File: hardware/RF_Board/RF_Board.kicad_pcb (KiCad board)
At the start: 4 copper layers, 90 x 90 mm, 130 parts, among them J1 Conn_Coaxial, J2 Conn_01x04_Male, J3 Conn_Coaxial, J4 Conn_01x04_Male, J5 Conn_01x06_Female, J6 Conn_01x06_Female, J7 Conn_01x06_Female, J8 L77TSAH15SOL2RM8, Q1 2N7002, Q2 2N7002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

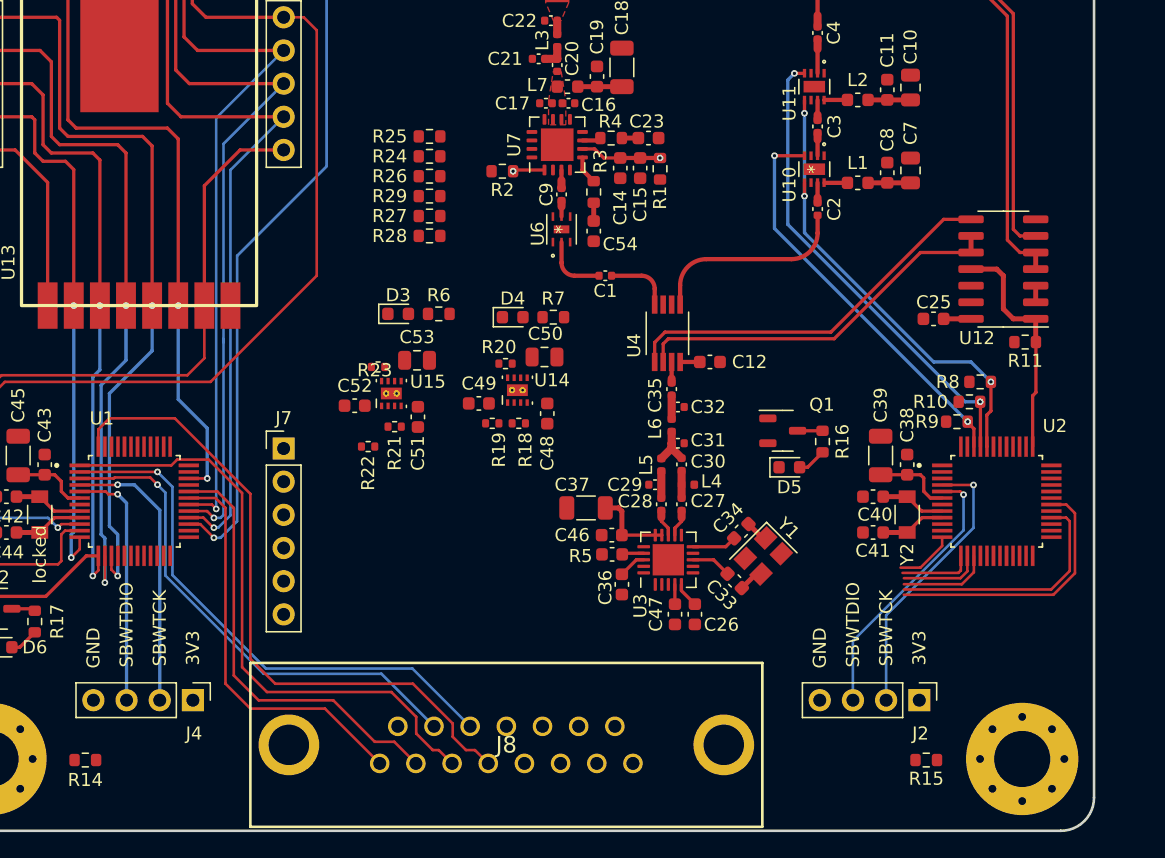
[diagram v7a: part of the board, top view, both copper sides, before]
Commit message: more RF board digital layout
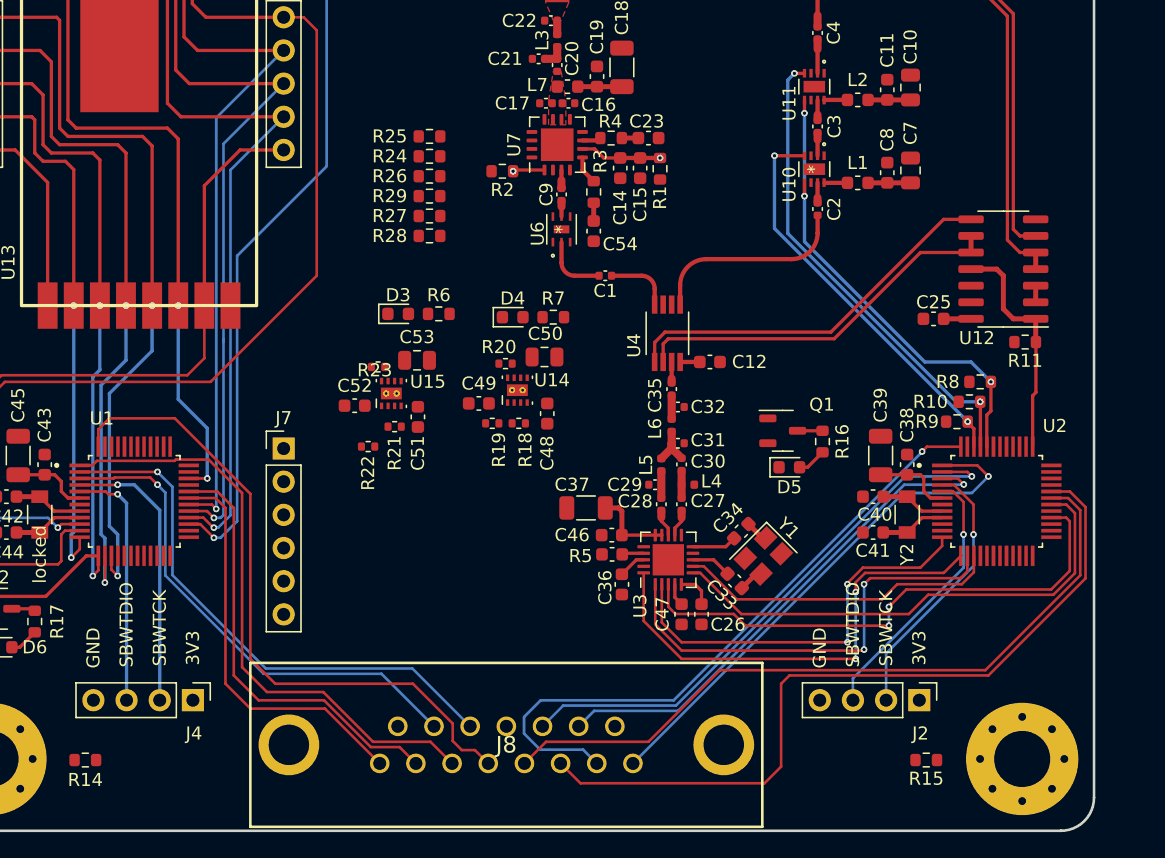
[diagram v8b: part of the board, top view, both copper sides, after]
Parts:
- moved C26 0.51 mm to (59.9, 73.4)
- moved C47 0.51 mm to (58.4, 73.4)
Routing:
- net /CC2500_UART_RX: track 0.00 -> 59.6 mm
- net /CC2500_UART_TX: track 0.00 -> 56.1 mm
- net /CC2500_TX_EMPTY: track 0.00 -> 49.8 mm, vias 0 -> 1
- net /CC2500_TX_OVERFLOW: track 0.00 -> 43.2 mm, vias 0 -> 1
- net /CC2500_RX_EMPTY: track 0.00 -> 40.2 mm, vias 0 -> 1
- net /CC2500_RX_OVERFLOW: track 0.00 -> 39.0 mm, vias 0 -> 1
- net /CC2500_MOSI: track 5.75 -> 36.0 mm, vias 0 -> 2
- net /CC2500_SCLK: track 6.26 -> 34.4 mm, vias 0 -> 2
- net /CC2500_MISO: track 4.54 -> 31.4 mm, vias 0 -> 2
- net /GDO2: track 18.6 -> 41.0 mm, vias 0 -> 2
- net /GDO0: track 20.5 -> 38.5 mm
- net /CC2500_CSN: track 6.99 -> 24.7 mm
- net /CC2500_SBWTCK: track 21.7 -> 20.8 mm
- net Net-(C26-Pad1): track 1.93 -> 2.76 mm
- net /RFM_TX_EMPTY: track 46.9 -> 46.1 mm
